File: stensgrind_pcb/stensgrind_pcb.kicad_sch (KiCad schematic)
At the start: 84 parts, among them J1 Conn_01x04_Pin, J2 SERIAL_01, J3 DISPLAY_01, SW1 SW_PUSH, SW10 SW_PUSH, SW11 SW_PUSH, SW12 SW_PUSH, SW13 SW_PUSH, SW14 SW_PUSH, SW15 SW_PUSH, SW16 SW_PUSH, SW17 SW_PUSH, SW18 SW_PUSH, SW19 SW_PUSH, SW2 SW_PUSH, SW20 SW_PUSH, SW21 SW_PUSH, SW22 SW_PUSH, SW23 SW_PUSH, SW3 SW_PUSH, SW4 SW_PUSH, SW5 SW_PUSH, SW6 SW_PUSH, SW7 SW_PUSH, SW8 SW_PUSH, SW9 SW_PUSH, U1 ProMicro_r, U10 4492, U11 4492, U12 4492, U13 4492, U14 4492, U15 4492, U16 4492, U17 4492, U18 4492, U19 4492, U2 CAHCT1G125QDCKRQ1, U20 4492, U21 4492, U22 4492, U23 4492, U24 4492, U25 4492, U26 ISO1050DUB, U3 4492, U4 4492, U5 4492, U6 4492, U7 4492, U8 4492, U9 4492

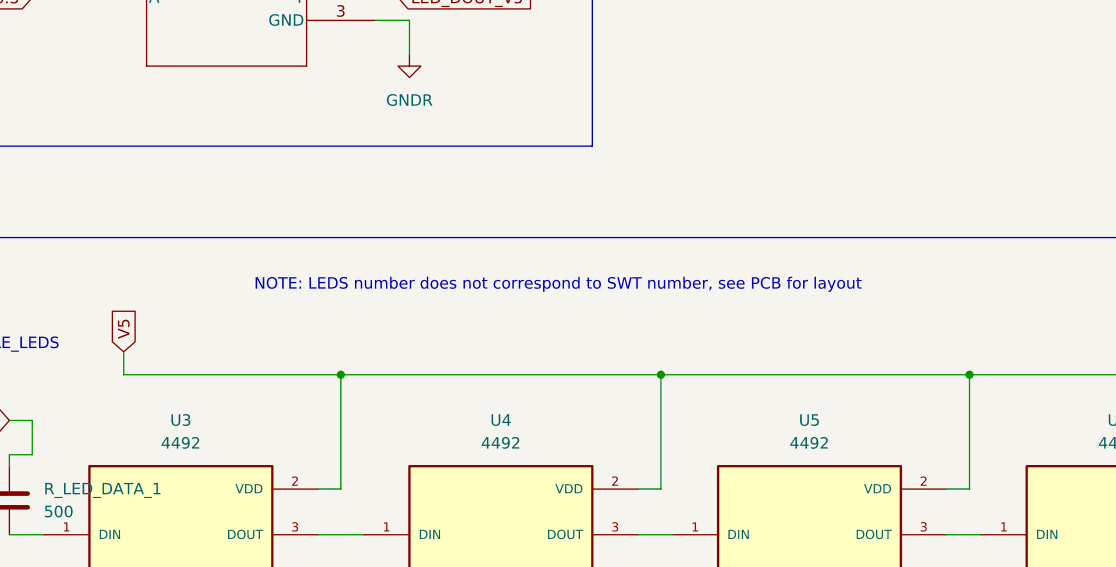
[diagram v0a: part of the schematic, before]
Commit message: Keep switch name consistent
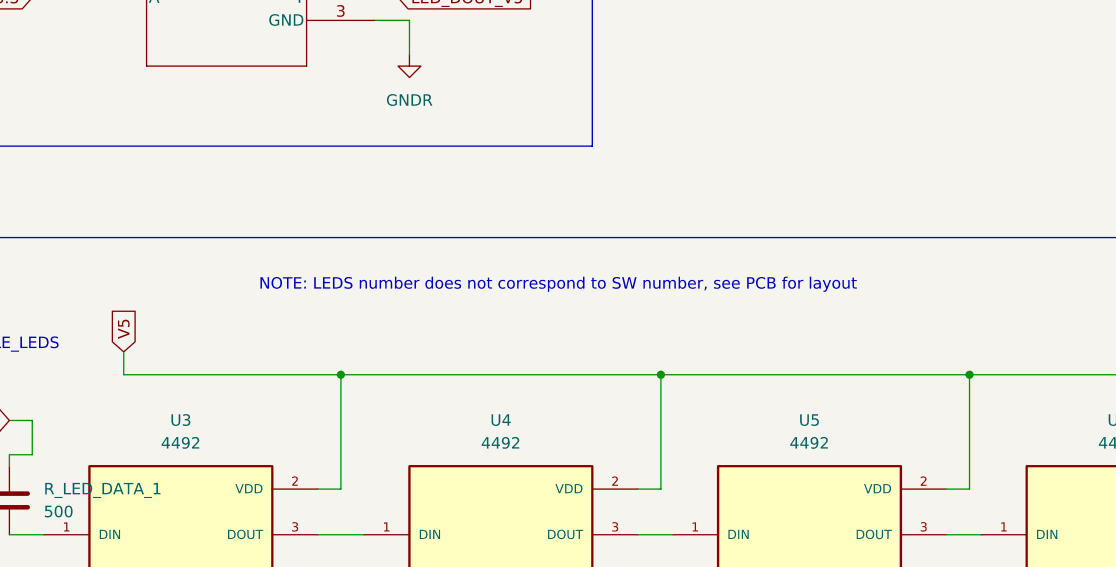
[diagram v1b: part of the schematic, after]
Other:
- note added: "NOTE: LEDS number does not correspond to SW number, see PCB for layout"
- note removed: "NOTE: LEDS number does not correspond to SWT number, see PCB for layout"
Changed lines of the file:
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@@
 		)
 	)
-	(text "NOTE: LEDS number does not correspond to SWT number, see PCB for layout"
+	(text "NOTE: LEDS number does not correspond to SW number, see PCB for layout"
 		(exclude_from_sim no)
 		(at 350.52 109.474 0)

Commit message: add right half
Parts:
- removed C1, C2: 0.1uf, Capacitor_SMD:C_0805_2012Metric_Pad1.18x1.45mm_HandSolder, symbol Device:C
- removed D1, D10, D11, D12, D13, D14, D15, D16, D17, D18, D19, D2, D20, D21, D22, D23, D3, D4, D5, D6, D7, D8, D9: D, Diode_THT:D_DO-35_SOD27_P10.16mm_Horizontal, symbol Device:D
- removed J1: Conn_01x04_Pin, Connector_PinSocket_2.54mm:PinSocket_1x04_P2.54mm_Vertical, symbol Connector:Conn_01x04_Pin
- removed J2: SERIAL_01, Connector_PinSocket_2.54mm:PinSocket_1x03_P2.54mm_Vertical, symbol Connector:Conn_01x03_Pin
- removed J3: DISPLAY_01, Connector_PinSocket_2.54mm:PinSocket_1x04_P2.54mm_Vertical, symbol Connector:Conn_01x04_Pin
- removed R1, R2, R5, R6: 100k, Resistor_SMD:R_1206_3216Metric_Pad1.30x1.75mm_HandSolder, symbol Device:R
- removed R3: 120, Resistor_SMD:R_1206_3216Metric_Pad1.30x1.75mm_HandSolder, symbol Device:R
- removed R_LED_DATA_1, R_LED_DATA_2: 500, Resistor_SMD:R_1206_3216Metric_Pad1.30x1.75mm_HandSolder, symbol Device:C
- removed SW1, SW10, SW11, SW12, SW13, SW14, SW15, SW16, SW17, SW18, SW19, SW2, SW20, SW21, SW22, SW23, SW3, SW4, SW5, SW6, SW7, SW8, SW9: SW_PUSH, kbd:keyswitch_cherrymx_hotswap_1u, symbol kbd:SW_PUSH
- removed U1: ProMicro_r, kbd:ProMicro, symbol kbd:ProMicro_r
- removed U10, U11, U12, U13, U14, U15, U16, U17, U18, U19, U20, U21, U22, U23, U24, U25, U3, U4, U5, U6, U7, U8, U9: 4492, DEV_18288:LED_4492, symbol DEV-18288:4492
- removed U2: CAHCT1G125QDCKRQ1, DEV_18288:DCK5, symbol DEV-18288:CAHCT1G125QDCKRQ1
- removed U26: ISO1050DUB, Package_SO:SOP-8_6.62x9.15mm_P2.54mm, symbol Interface_CAN_LIN:ISO1050DUB
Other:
- added sheet LEFT_SIDE (left.kicad_sch)
- added sheet RIGHT_SIDE (right.kicad_sch)
- note removed: "ADDRESSABLE_LEDS"
- note removed: "CAN TRANCIEVER"
- note removed: "CONTROLLER"
- note removed: "CONVERT LED CONTROL SIGNAL FROM 3.3V to 5V"
- note removed: "DISPLAY"
- note removed: "NOTE: LEDS number does not correspond to SW number, see PCB for layout"
- note removed: "SERIAL_DEBUG"
- note removed: "SWITCH MATRIX"
